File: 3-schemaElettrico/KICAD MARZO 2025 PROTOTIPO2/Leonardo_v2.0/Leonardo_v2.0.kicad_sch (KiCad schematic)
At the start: 8 parts, among them J1 Screw_Terminal_01x02, J2 Conn_01x06_Pin, J3 Conn_01x06_Pin, J4 Conn_01x04_Pin, J5 Conn_01x04_Pin, J6 Conn_01x04_Pin, J7 Conn_01x04_Pin

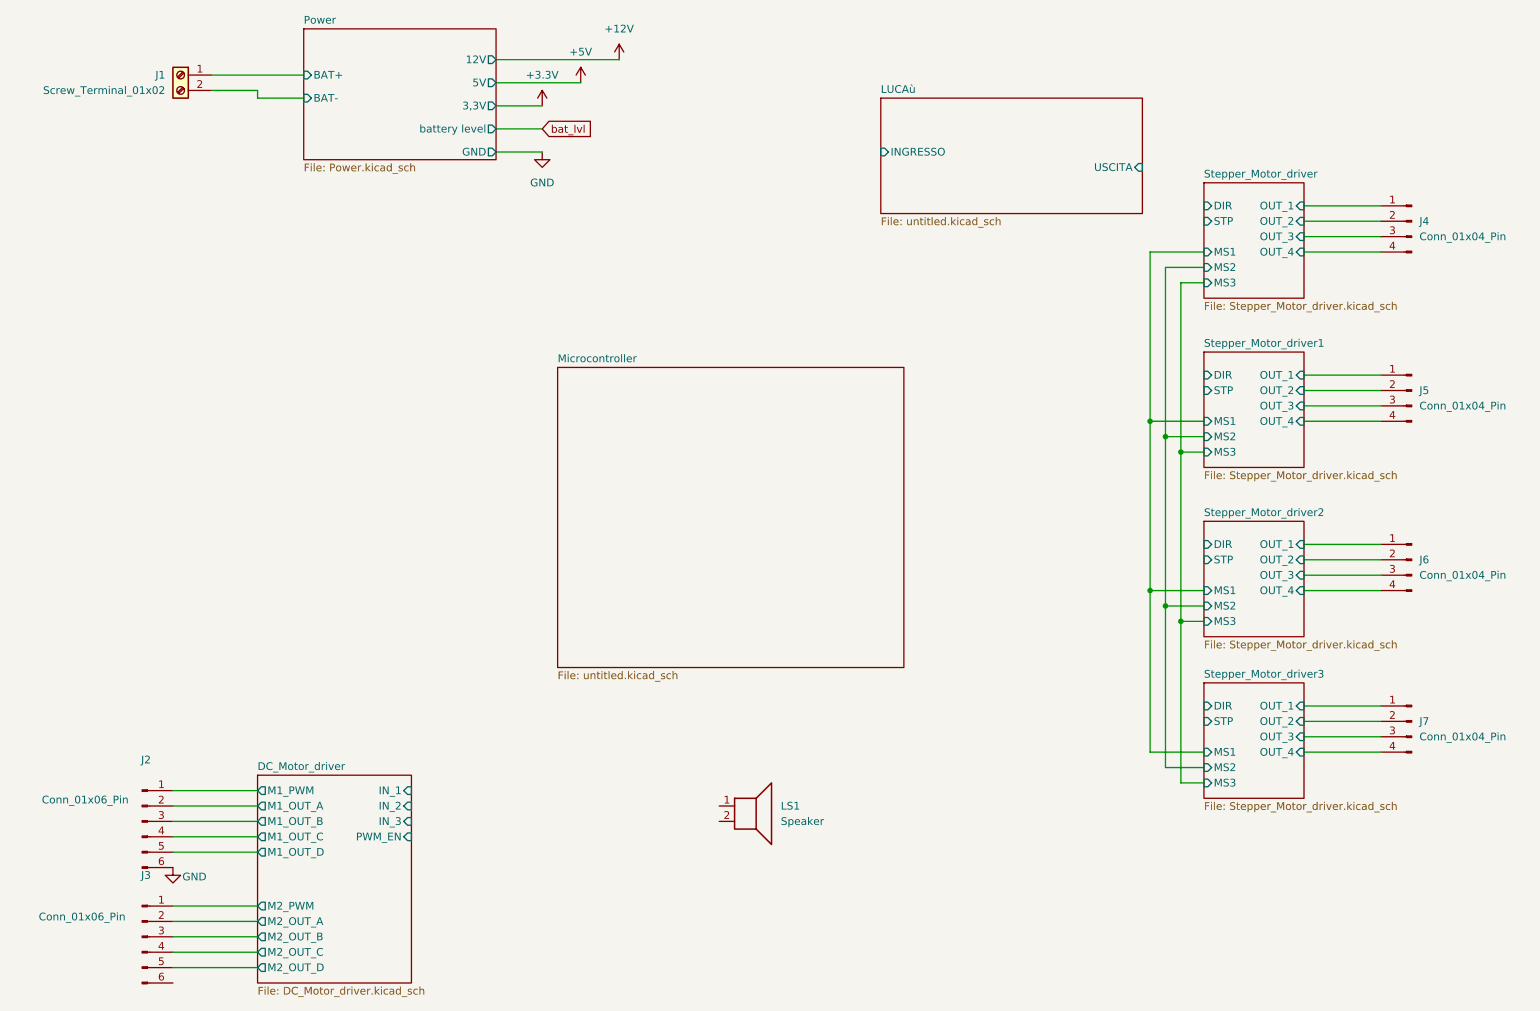
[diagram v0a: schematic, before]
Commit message: done 74hc238
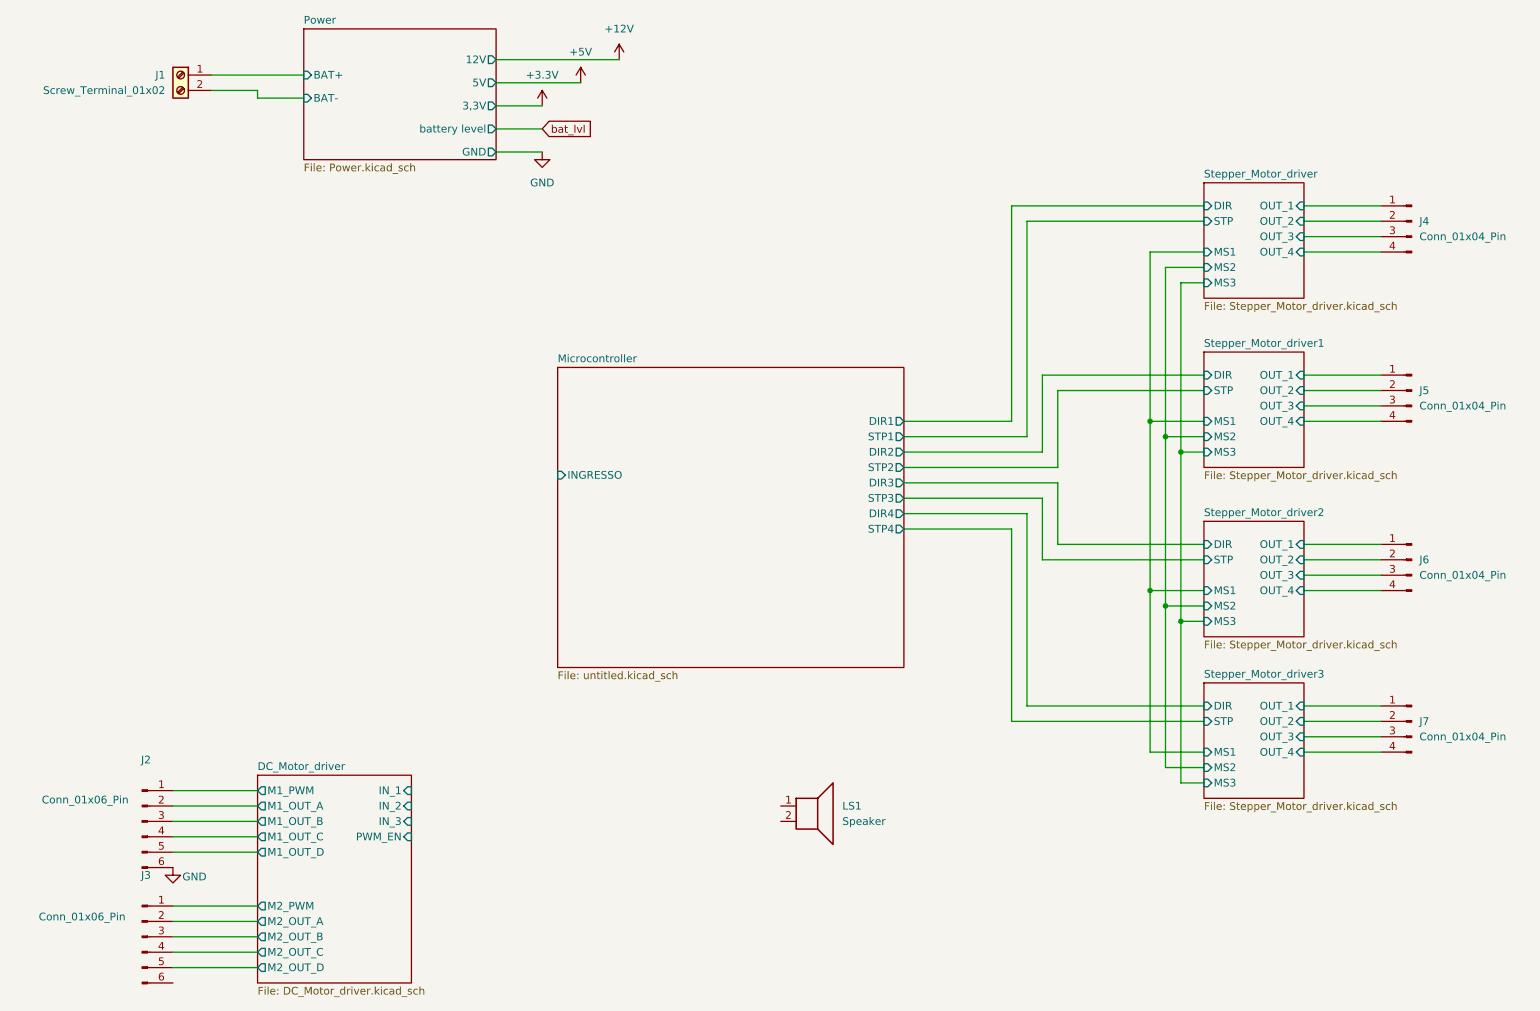
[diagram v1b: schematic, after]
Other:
- removed sheet LUCAù
- sheet Microcontroller ports: added DIR1, DIR2, DIR3, DIR4, INGRESSO, STP1, STP2, STP3, STP4; removed none
- moved on the sheet: LS1
